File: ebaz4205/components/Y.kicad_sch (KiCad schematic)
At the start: 1 part

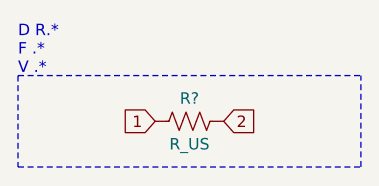
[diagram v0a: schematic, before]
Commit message: Provided all component symbols.
Symbol libraries are available as subdirectories in ebaz4205/components/

U23 is still unknown, so a placeholder symbol was provided.
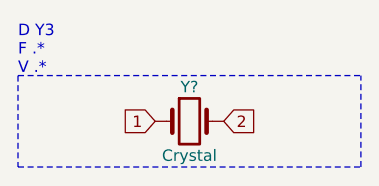
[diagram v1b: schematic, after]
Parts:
- removed R?: R_US, symbol Device:R_US
- added Y?: Crystal, symbol Device:Crystal
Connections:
- net 1: now also Y?.1
- net 2: now also Y?.2
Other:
- note added: "D Y3 F .* V .*"
- note removed: "D R.* F .* V .*"
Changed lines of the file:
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@@
     (stroke (width 0) (type dash) (color 0 0 0 0))
   )
-  (text "D R.*\nF .*\nV .*" (at 0 0 0)
+  (text "D Y3\nF .*\nV .*" (at 0 0 0)
     (effects (font (size 1.27 1.27)) (justify left bottom))
   )
@@
     (effects (font (size 1.27 1.27)) (justify left))
   )
-  (symbol (lib_id "Device:R_US") (at 19.05 5.08 90) (unit 1)
+  (symbol (lib_id "Device:Crystal") (at 19.05 5.08 0) (unit 1)
     (in_bom yes) (on_board yes)
-    (property "Reference" "R?" (id 0) (at 19.05 2.54 90))
-    (property "Value" "R_US" (id 1) (at 19.05 7.62 90))
-    (property "Footprint" "" (id 2) (at 19.304 4.064 90)
+    (property "Reference" "Y?" (id 0) (at 19.05 1.27 0))
+    (property "Value" "Crystal" (id 1) (at 19.05 8.89 0))
+    (property "Footprint" "" (id 2) (at 19.05 5.08 0)
       (effects (font (size 1.27 1.27)) hide)
     )
@@
   )
   (symbol_instances
-    (path "/93a03812-9ad2-4f98-81ae-a8c92d489812"
-      (reference "R?") (unit 1) (value "R_US") (footprint "")
+    (path "/4f850b9a-822a-4df9-a56a-22a2bd0cd62e"
+      (reference "Y?") (unit 1) (value "Crystal") (footprint "")
     )
   )
